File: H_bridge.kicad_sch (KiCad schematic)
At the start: 32 parts, among them J1 Conn_01x02_Female, T3 AOD4132, T4 AOD4132, T5 AOD4132, T6 AOD4132, U1 IR2104, U2 IR2104

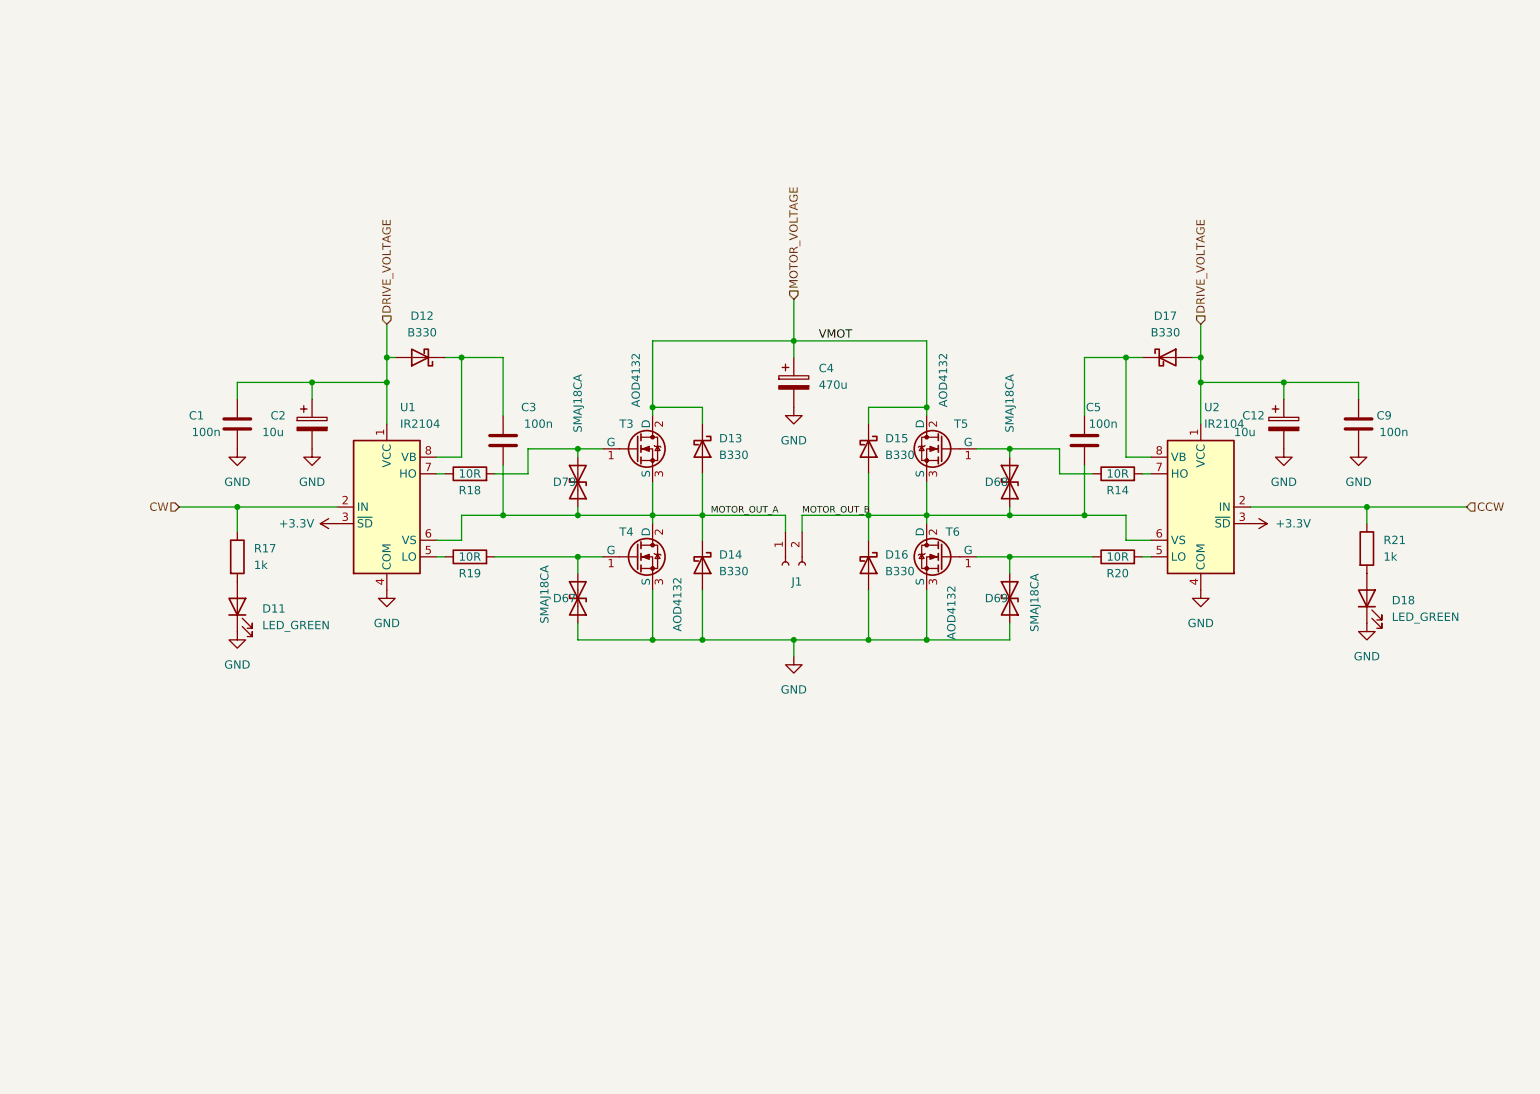
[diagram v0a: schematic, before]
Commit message: added motor rotate hall sensor translator circuit in H-bridge modules, hierarchical schematic layout visual correction due to add HALL_OUT output
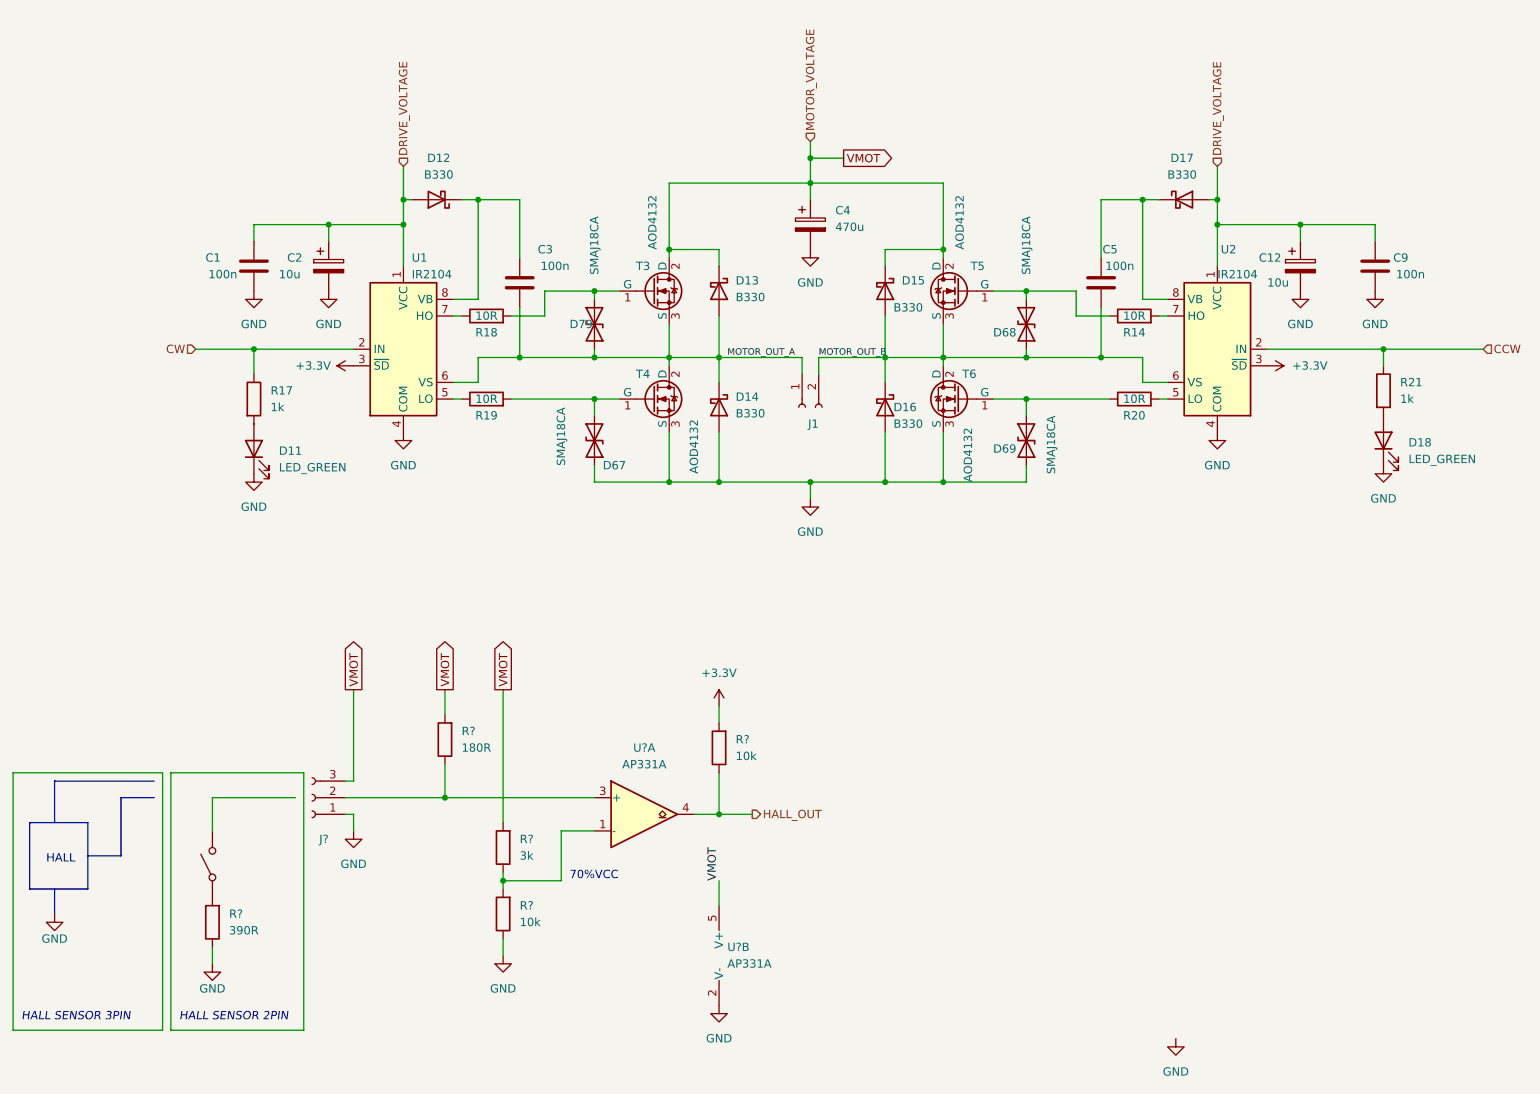
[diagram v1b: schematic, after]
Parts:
- added J?: Conn_01x03_Female, symbol Connector:Conn_01x03_Female
- added R?: 3k, Resistor_SMD:R_0603_1608Metric_Pad0.98x0.95mm_HandSolder, symbol Device:R
- added R?: 180R, Resistor_SMD:R_0603_1608Metric_Pad0.98x0.95mm_HandSolder, symbol Device:R
- added R? (x2): 10k, Resistor_SMD:R_0603_1608Metric_Pad0.98x0.95mm_HandSolder, symbol Device:R
- added R?: 390R, Resistor_SMD:R_0603_1608Metric_Pad0.98x0.95mm_HandSolder, symbol Device:R
- added SW?: SW_SPST, symbol Switch:SW_SPST
- added U? (x2): AP331A, symbol _IntegratedCircuits:AP331A
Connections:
- net +3V3: now also R?.2
- net GND: now also J?.1 (Pin_1), R?.1, R?.1, U?.2 (V-)
- net MOTOR_VOLTAGE renamed VMOT
- net VMOT: now also J?.3 (Pin_3), R?.2, R?.2, U?.5 (V+)
- new net: R?.1, R?.2, U?.1 (-)
- new net: J?.2 (Pin_2), R?.1, U?.3 (+)
- new net: R?.2, SW?.1 (A)
- new net HALL_OUT: R?.1, U?.4
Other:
- note added: "70%VCC"
- note added: "HALL"
- note added: "HALL SENSOR 2PIN"
- note added: "HALL SENSOR 3PIN"
- moved on the sheet: C1, C12, C2, C3, C4, C5, C9, D11, D12, D13, D14, D15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

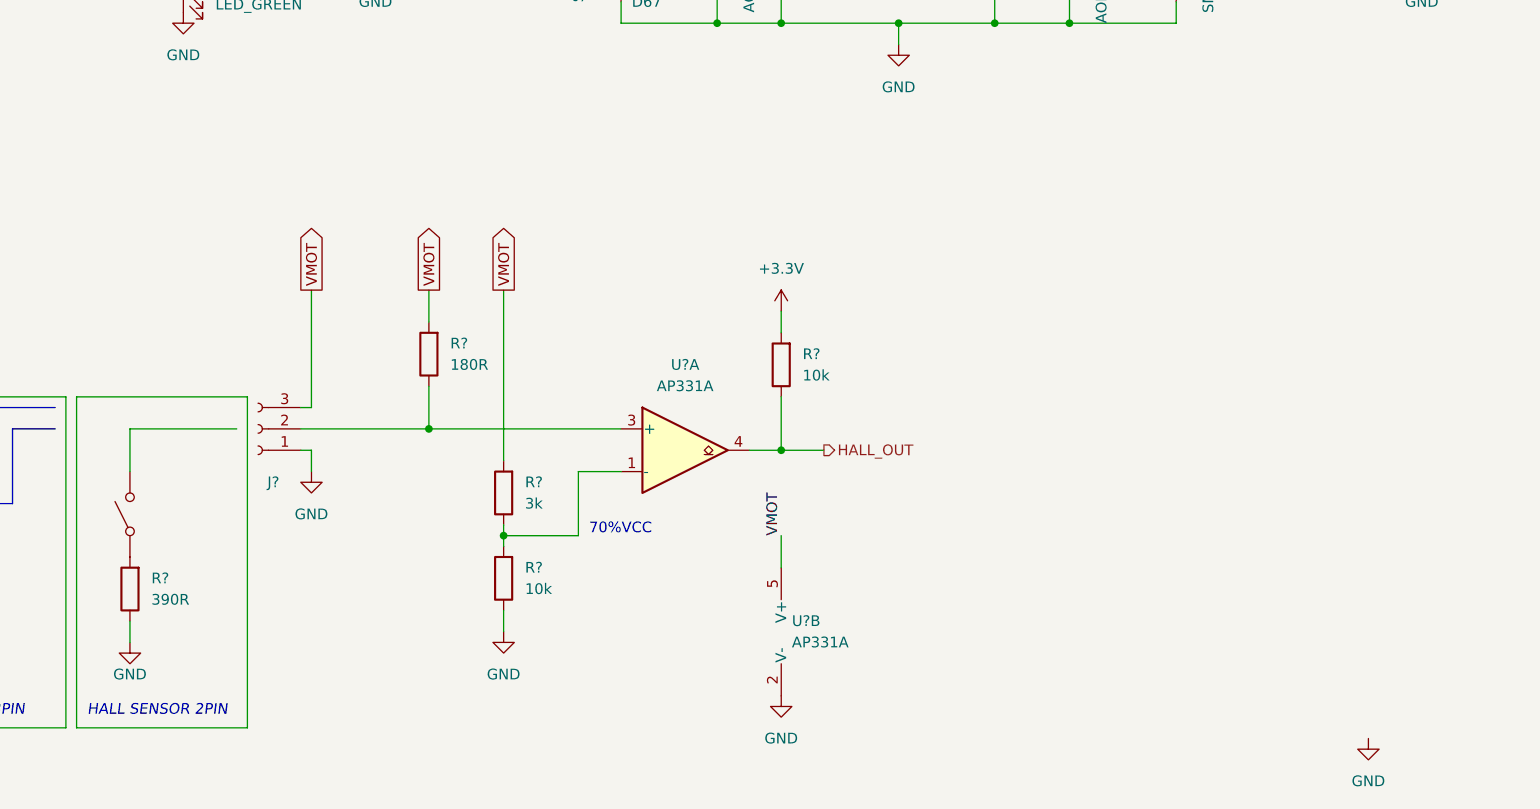
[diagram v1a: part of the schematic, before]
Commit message: add EEPROM funcionality, created new hierarchical sheet
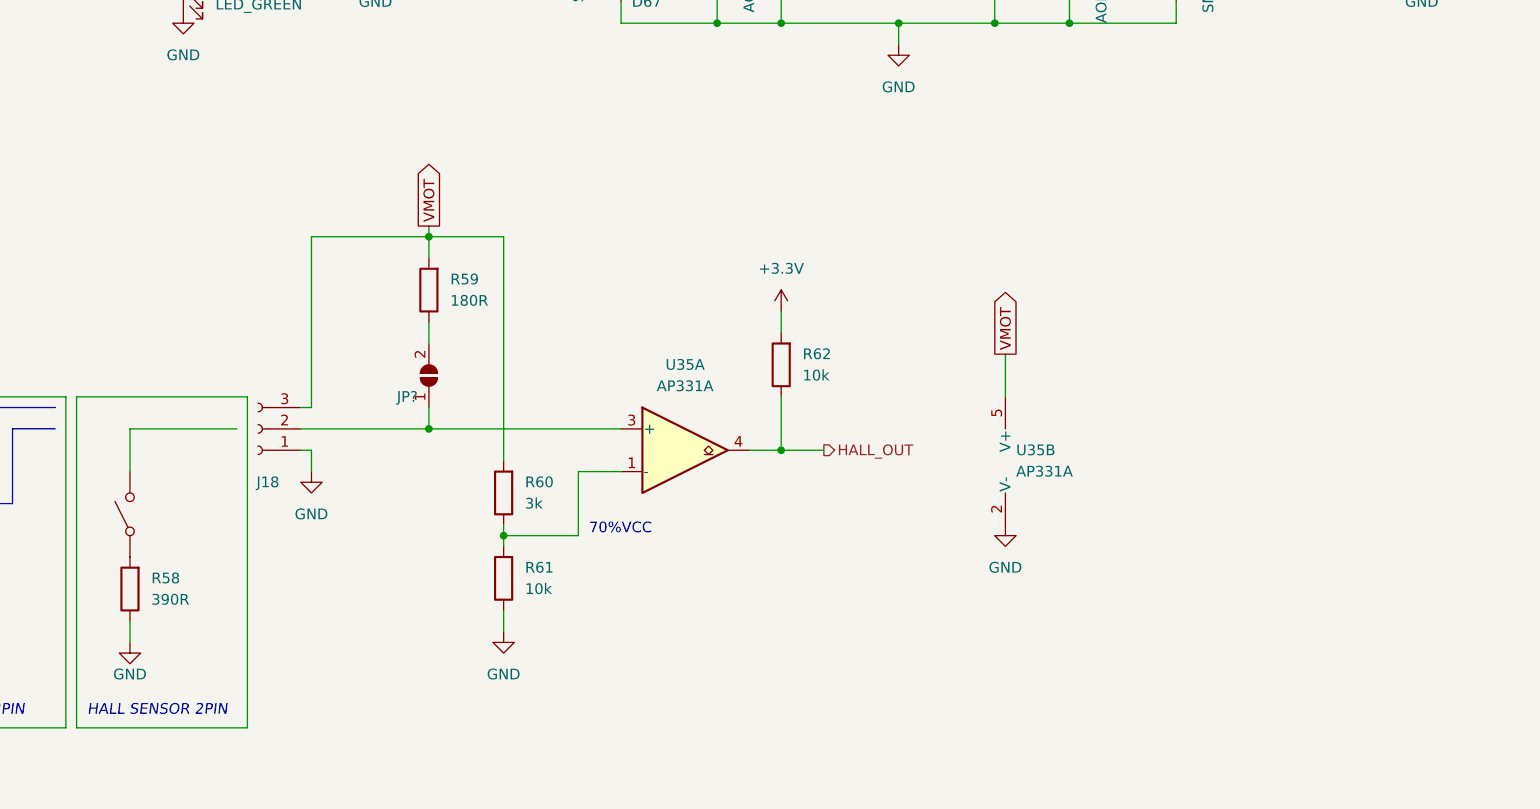
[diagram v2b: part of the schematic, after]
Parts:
- added JP?: SolderJumper_2_Open, symbol Jumper:SolderJumper_2_Open
- gave numbers to parts that had none: 8
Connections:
- net at J18.2 (Pin_2), U35.3 (+): now also JP?.1 (A); no longer R59.1
- new net: JP?.2 (B), R59.1
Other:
- moved on the sheet: R59, U35B

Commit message: added power loss detection, preparing for new pcb layout
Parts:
- D12, D13, D14, D15, D16, D17: footprint Diode_SMD:D_SMA_Handsoldering -> Diode_SMD:D_SMC
- D67, D68, D69, D79: footprint Diode_SMD:D_SMA_Handsoldering -> Diode_THT:D_DO-201AE_P15.24mm_Horizontal
- J18: footprint (none) -> TerminalBlock_Phoenix:TerminalBlock_Phoenix_MKDS-1,5-3-5.08_1x03_P5.08mm_Horizontal
- JP2: renamed from JP?; footprint (none) -> Jumper:SolderJumper-2_P1.3mm_Open_TrianglePad1.0x1.5mm
- U35: footprint (none) -> _IntegratedCircuits:AP331A
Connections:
- net VMOT renamed MOTOR_VOLTAGE
- no-connect marks 0 -> 1
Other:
- note added: "GND"
